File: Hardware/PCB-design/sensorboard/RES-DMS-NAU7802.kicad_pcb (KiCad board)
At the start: 2 copper layers, 32 x 32 mm, 43 parts, among them J1 Conn_01x06, J2 straingauge, J3 straingauge, J4 straingauge, J5 straingauge, J6 straingauge, J7 straingauge, J8 straingauge, J9 straingauge, U1 NAU7802-SGI

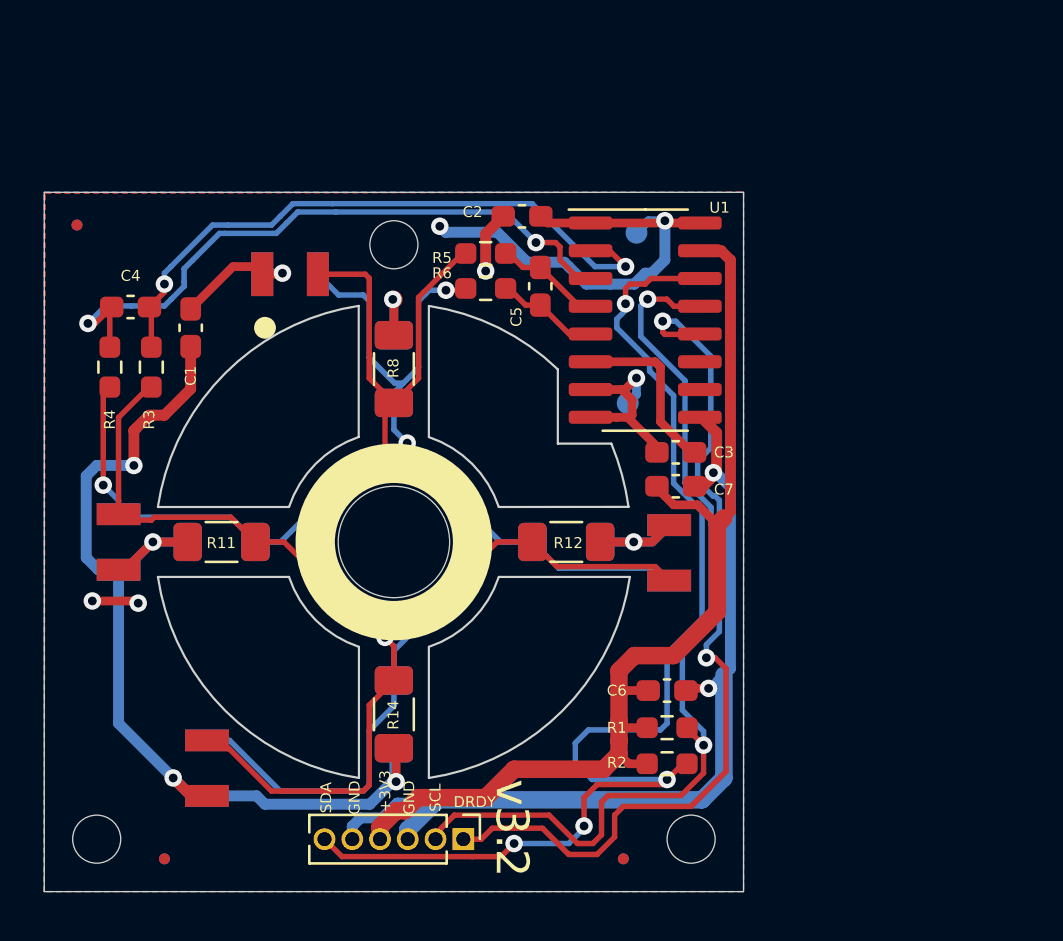
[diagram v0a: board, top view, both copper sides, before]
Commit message: Changed to v3.3 layout with DMS & possibility for resistors. Changed to 4 hole design again.
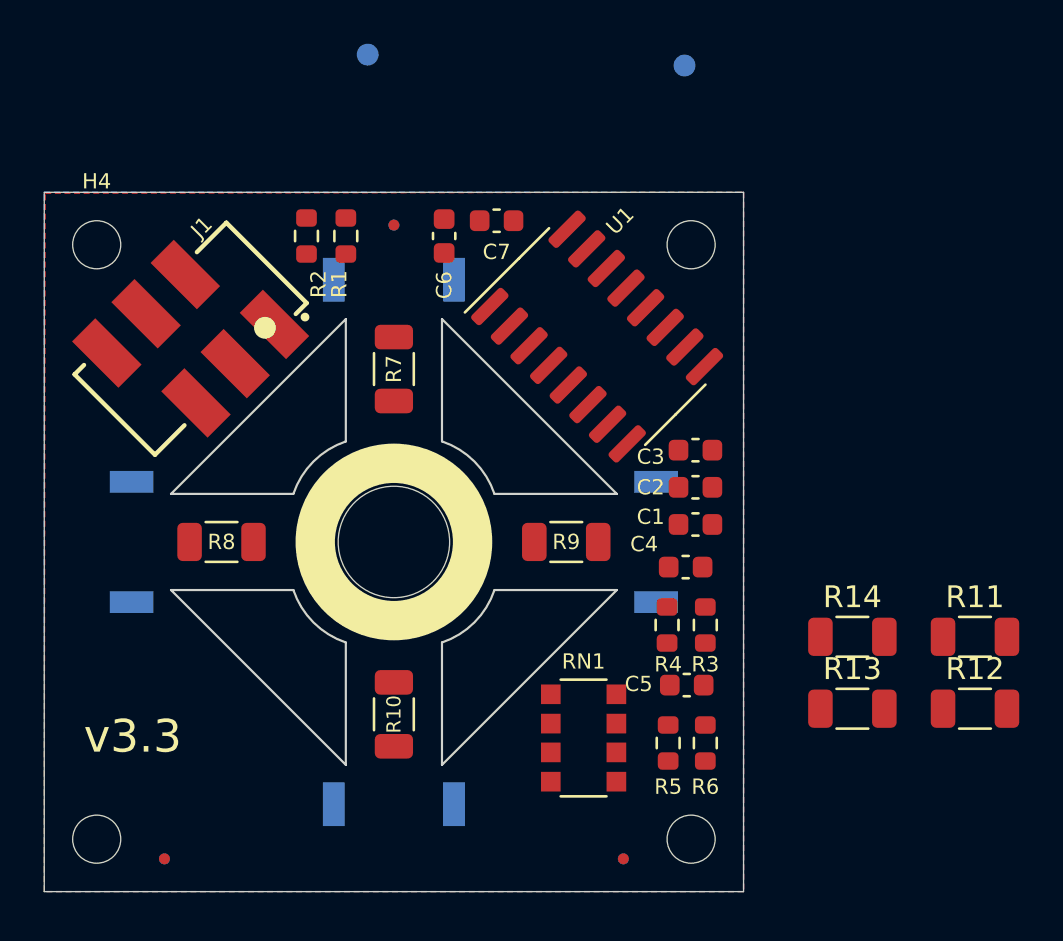
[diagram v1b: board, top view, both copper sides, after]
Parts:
- removed J3, J7, J9: straingauge, Project:straingauges
- removed the J6 at (103.4, 104.0)
- removed the R10 at (123.9, 104.0)
- removed the R7 at (116.0, 96.1)
- removed the R9 at (108.1, 104.0)
- added H4: MountingHole, MountingHole:MountingHole_2.2mm_M2_DIN965, F.Cu at (102.4, 90.4)
- added LOGO2: WEEE-Logo, Symbol:WEEE-Logo_4.2x6mm_SilkScreen, B.Cu at (128.9, 111.5)
- added LOGO3: CE-Logo, Symbol:CE-Logo_8.5x6mm_SilkScreen, B.Cu at (108.2, 91.8)
- added R11: 1k, Resistor_SMD:R_1206_3216Metric, F.Cu at (142.6, 108.3)
- added R12: 1k, Resistor_SMD:R_1206_3216Metric, F.Cu at (142.6, 111.6)
- added R14: 1k, Resistor_SMD:R_1206_3216Metric, F.Cu at (137.0, 108.3)
- added RN1: R_Pack04, Resistor_SMD:R_Array_Convex_4x1206, F.Cu at (124.7, 113.0)
- C1, C2, C3, C4, C5, C6, C7: footprint Capacitor_SMD:C_0603_1608Metric_Pad1.08x0.95mm_HandSolder -> Capacitor_SMD:C_0603_1608Metric
- J1: footprint Connector_PinHeader_1.27mm:PinHeader_1x06_P1.27mm_Vertical -> Project:690367280676
- R1, R2, R3, R4, R5, R6: footprint Resistor_SMD:R_0603_1608Metric_Pad0.98x0.95mm_HandSolder -> Resistor_SMD:R_0603_1608Metric
- R10: renamed from R14; footprint Resistor_SMD:R_1206_3216Metric_Pad1.30x1.75mm_HandSolder -> Resistor_SMD:R_1206_3216Metric
- R13: footprint Resistor_SMD:R_1206_3216Metric_Pad1.30x1.75mm_HandSolder -> Resistor_SMD:R_1206_3216Metric; moved to F.Cu
- R7: renamed from R8; footprint Resistor_SMD:R_1206_3216Metric_Pad1.30x1.75mm_HandSolder -> Resistor_SMD:R_1206_3216Metric
- R8: renamed from R11; footprint Resistor_SMD:R_1206_3216Metric_Pad1.30x1.75mm_HandSolder -> Resistor_SMD:R_1206_3216Metric
- R9: renamed from R12; footprint Resistor_SMD:R_1206_3216Metric_Pad1.30x1.75mm_HandSolder -> Resistor_SMD:R_1206_3216Metric
- moved R2 29.2 mm to (112.0, 90.0), turned to -90 degrees
- moved R4 28.1 mm to (128.5, 107.8)
- moved C4 28.0 mm to (129.3, 105.2)
- moved R3 28.0 mm to (130.2, 107.8)
- moved R1 26.9 mm to (113.8, 90.0), turned to -90 degrees
- moved J1 26.1 mm to (106.7, 94.7), turned to -135 degrees
- moved C1 24.8 mm to (129.8, 103.2), turned to 180 degrees
- moved R5 23.9 mm to (128.6, 113.2), turned to -90 degrees
- moved C6 23.2 mm to (118.3, 90.0), turned to 90 degrees
- moved R6 23.1 mm to (130.2, 113.2), turned to -90 degrees
- moved R13 21.0 mm to (137.0, 111.6), turned to 0 degrees
- moved TP1 19.9 mm to (114.8, 81.7)
- moved C5 19.4 mm to (129.4, 110.5), turned to 180 degrees
- moved C2 14.7 mm to (129.8, 101.5)
- moved C7 14.7 mm to (120.7, 89.3), turned to 180 degrees
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- renumbered J8 to J6
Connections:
- R10 pad 1: /V3 -> /V4
- R13 pad 1: /V4 -> +3.3VADC
- R13 pad 2: +3.3VADC -> /V3
- R7 pad 2: /V3 -> /V4
- R8 pad 2: /V1 -> /V2
- R9 pad 1: /V1 -> /V2
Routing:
- net +3.3VADC: track 71.5 -> 0.00 mm, vias 6 -> 0
- net /SDA: track 55.4 -> 0.00 mm, vias 4 -> 0
- net +3.3V: track 47.9 -> 0.00 mm
- net /V3: track 47.1 -> 0.00 mm, vias 2 -> 0
- net /V4: track 44.8 -> 0.00 mm, vias 3 -> 0
- net /SCL: track 43.4 -> 0.00 mm, vias 2 -> 0
- net GND: track 41.1 -> 0.00 mm, vias 2 -> 0
- net /DRDY: track 40.6 -> 0.00 mm, vias 2 -> 0
- net /V1: track 35.8 -> 0.00 mm
- net /V2: track 35.6 -> 0.00 mm, vias 1 -> 0
- net GNDA: track 30.5 -> 0.00 mm, vias 7 -> 0
- net Net-(C4-Pad1): track 30.5 -> 0.00 mm, vias 2 -> 0
- net Net-(C4-Pad2): track 29.2 -> 0.00 mm, vias 2 -> 0
- net Net-(C3-Pad2): track 7.94 -> 0.00 mm
- net Net-(C5-Pad2): track 4.95 -> 0.00 mm
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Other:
- outline, holes or cut-outs redrawn
- board text added: "RES-DMS v3.3 NAU7802 Aigner 01.2023"
- board text added: "v3.3"
- board text removed: "+3V3"
- board text removed: "DRDY"
- board text removed: "GND"
- board text removed: "RES-DMS v3.2 NAU7802 Aigner 11.2022"
- board text removed: "SCL"
- board text removed: "SDA"
- board text removed: "v3.2"

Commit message: Routed DMS board
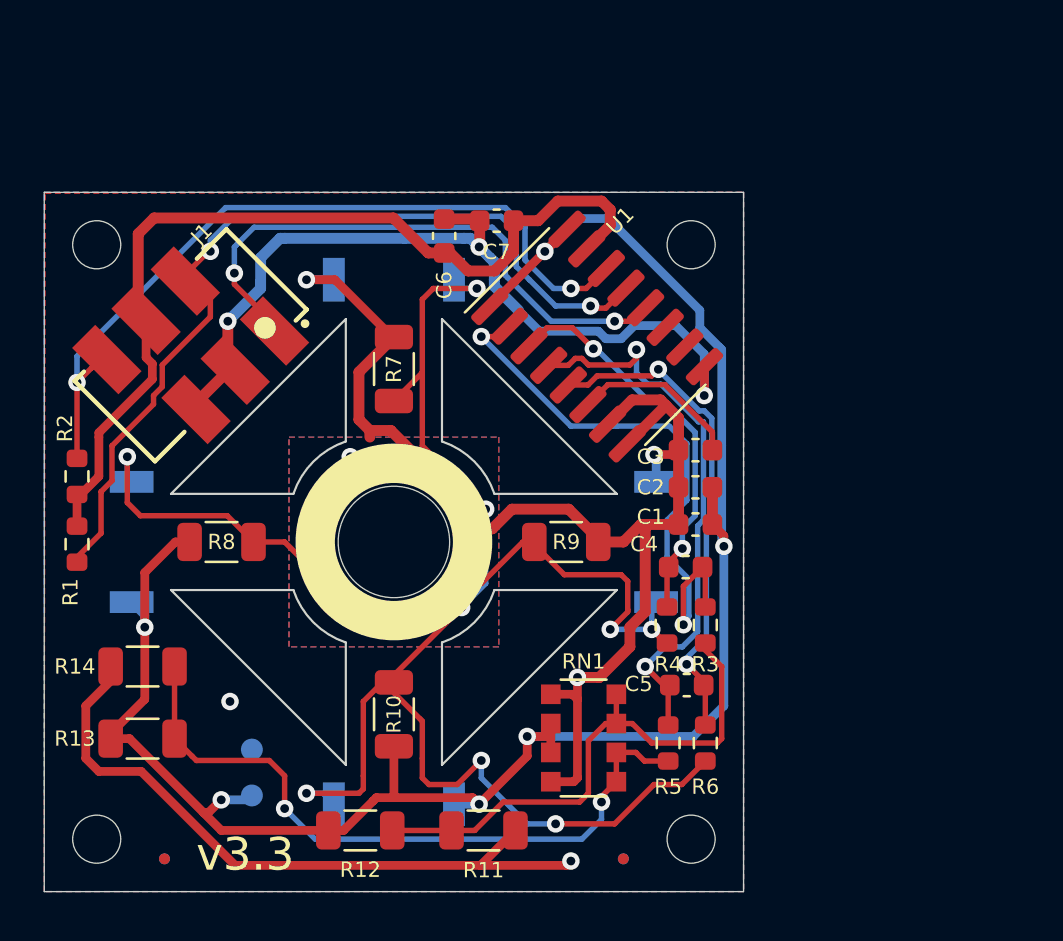
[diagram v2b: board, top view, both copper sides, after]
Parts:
- moved TP2 38.8 mm to (109.5, 115.6)
- moved R13 32.5 mm to (104.5, 113.0)
- moved R14 32.5 mm to (104.5, 109.7)
- moved TP1 32.2 mm to (109.5, 113.5)
- moved R12 28.7 mm to (114.5, 117.2)
- moved R11 24.2 mm to (120.1, 117.2), turned to 180 degrees
- moved R1 18.7 mm to (101.5, 104.1)
- moved R2 15.2 mm to (101.5, 101.0), turned to 90 degrees
- moved FID1 10.6 mm to (116.0, 100.1)
- moved FID5 10.6 mm to (116.0, 100.1)
- moved J1 0.30 mm to (106.7, 95.0)
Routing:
- net GNDA: track 0.00 -> 90.9 mm, vias 0 -> 6
- net +3.3VADC: track 0.00 -> 89.7 mm, vias 0 -> 6
- net /V4: track 0.00 -> 57.4 mm, vias 0 -> 6
- net +3.3V: track 0.00 -> 42.5 mm
- net /SCL: track 0.00 -> 40.8 mm, vias 0 -> 2
- net GND: track 0.00 -> 38.3 mm, vias 0 -> 3
- net /V2: track 0.00 -> 37.9 mm, vias 0 -> 3
- net /SDA: track 0.00 -> 36.4 mm, vias 0 -> 2
- net /V3: track 0.00 -> 31.9 mm, vias 0 -> 2
- net Net-(C4-Pad2): track 0.00 -> 27.0 mm, vias 0 -> 2
- net /DRDY: track 0.00 -> 26.5 mm, vias 0 -> 2
- net Net-(C5-Pad2): track 0.00 -> 26.0 mm, vias 0 -> 2
- net /V1: track 0.00 -> 25.0 mm
- net Net-(C5-Pad1): track 0.00 -> 22.7 mm, vias 0 -> 2
- net Net-(C4-Pad1): track 0.00 -> 18.4 mm, vias 0 -> 2
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- added copper zone on F.Cu, net GNDA
- removed copper zone on F.Cu, net +3.3VADC
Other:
- board text added: "GNDA"
- board text added: "VCCA"

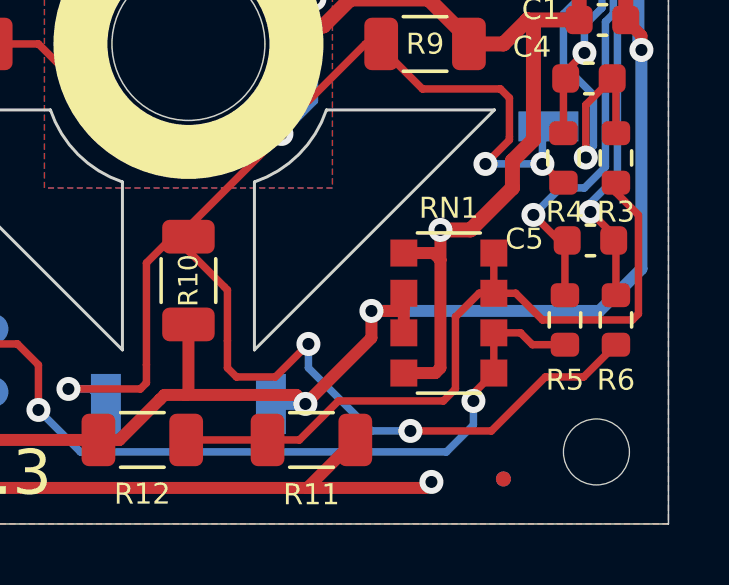
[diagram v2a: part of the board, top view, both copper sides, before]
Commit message: Changed resistor network footprint, was wrong.
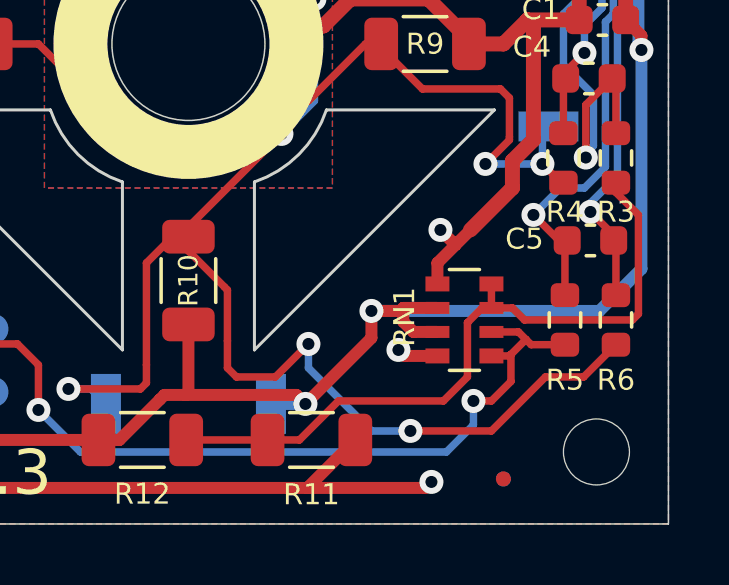
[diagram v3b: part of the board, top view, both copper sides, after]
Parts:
- RN1: footprint Resistor_SMD:R_Array_Convex_4x1206 -> Resistor_SMD:R_Array_Convex_4x0603
- moved RN1 0.57 mm to (125.2, 113.2)
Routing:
- net GNDA: track 90.9 -> 87.0 mm, vias 6 -> 7
- net +3.3VADC: track 89.7 -> 91.2 mm
- net /V3: track 31.9 -> 33.2 mm
- net /V1: track 25.0 -> 23.7 mm
